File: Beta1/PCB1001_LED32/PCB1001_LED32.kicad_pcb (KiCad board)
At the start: 2 copper layers, 188.9 x 15.5 mm, 164 parts, among them U0 APA102C, U1 APA102C, U10 APA102C, U11 APA102C, U12 APA102C, U13 APA102C, U14 APA102C, U15 APA102C, U16 APA102C, U17 APA102C, U18 APA102C, U19 APA102C, U2 APA102C, U20 APA102C, U21 APA102C, U22 APA102C, U23 APA102C, U24 APA102C, U25 APA102C, U26 APA102C, U27 APA102C, U28 APA102C, U29 APA102C, U3 APA102C, U30 APA102C, U31 APA102C, U4 APA102C, U5 APA102C, U6 APA102C, U7 APA102C, U8 APA102C, U9 APA102C

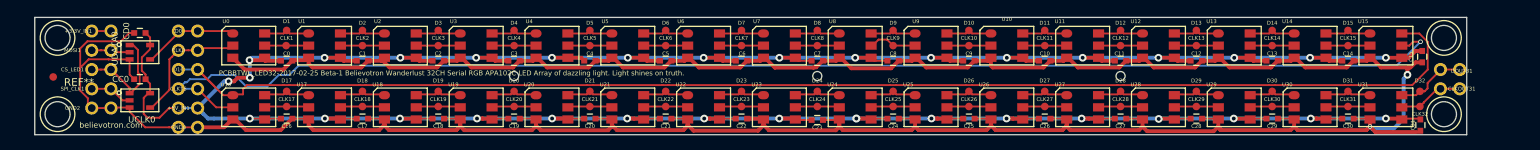
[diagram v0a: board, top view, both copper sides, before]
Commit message: Mid reroute. Move interference. Clean silk.
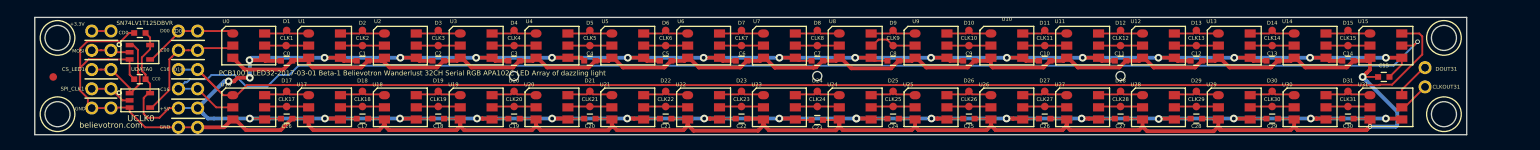
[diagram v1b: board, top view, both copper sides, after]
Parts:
- removed C31: 0.1u, Capacitors_SMD:C_0603
- removed CLK32, D32: CONN_01X01, Liberry:TESTPAD
- removed CLKOUTB31, DOUTB31: CONN_01X01, Liberry:single_0.1
- moved C15 5.73 mm to (180.5, -7.62), turned to 180 degrees
- moved CLKOUT31 2.05 mm to (185.8, -6.31)
- moved DOUT31 2.05 mm to (185.8, -8.67)
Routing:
- net GND: track 453.0 -> 443.0 mm
- net /D32: track 9.69 -> 5.15 mm
- net /CLK32: track 8.56 -> 4.39 mm
- net /D16: track 179.1 -> 176.6 mm
- net +5V: track 478.8 -> 476.8 mm
- net /CLK16: track 178.5 -> 177.7 mm
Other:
- board text added: "+3.3V"
- board text added: "+5V"
- board text added: "C00"
- board text added: "C16"
- board text added: "D00"
- board text added: "GND"
- board text added: "MOSI"
- board text added: "PCB1001_LED32-2017-03-01 Beta-1 Believotron Wanderlust 32CH Serial RGB APA102C LED Array of dazzling light"
- board text added: "Primary CS (Chip Select) wired to Micro To add downstream daisy chain PCBs Tie CS to GND Skip Buffers if using 5V logic"
- board text added: "SN74LV1T125DBVR"
- board text removed: "PCBBTWL_LED32-2017-02-25 Beta-1 Believotron Wanderlust 32CH Serial RGB APA102C LED Array of dazzling light. Light shines on truth."

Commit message: Added labels on bottom. Added CS short to GND.
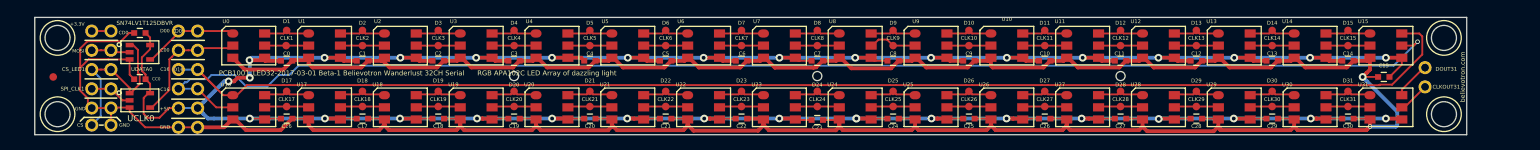
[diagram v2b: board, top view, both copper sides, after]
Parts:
- added CS_LED1: CONN_01X01, Liberry:single_0.1, F.Cu at (10.1, -1.27)
- added GNDB2: CONN_01X01, Liberry:single_0.1, F.Cu at (12.6, -1.27)
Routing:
- net Net-(CS_LED1-Pad1): track 14.5 -> 22.8 mm
- net GND: track 443.0 -> 445.3 mm
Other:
- board text added: "CS"
- board text added: "CS_LED1"
- board text added: "D16"
- board text added: "SPI_CLK_1"
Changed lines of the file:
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@@
 (kicad_pcb (version 4) (host pcbnew 4.0.4-stable)
   (general
-    (links 286)
-    (no_connects 0)
+    (links 282)
+    (no_connects 2)
     (area 2.489999 -15.524901 191.470001 0.050001)
     (thickness 1.6)
-    (drawings 35)
-    (tracks 771)
+    (drawings 52)
+    (tracks 776)
     (zones 0)
-    (modules 159)
+    (modules 161)
     (nets 73)
   )
@@
     (add_net "Net-(SPI_CLK1-Pad1)")
   )
+  (module Liberry:single_0.1 (layer F.Cu)
+    (at 12.59 -1.27)
+    (descr "10 pins through hole IDC header")
+    (tags "IDC header socket VASCH")
+    (fp_text reference GNDB2 (at -2.54 0) (layer F.SilkS) hide
+      (effects (font (size 0.5 0.5) (thickness 0.125)))
+    )
+    (fp_text value CONN_01X01 (at 0 2.54) (layer F.Fab)
+      (effects (font (size 1 1) (thickness 0.15)))
+    )
+    (pad 1 thru_hole circle (at 0 0) (size 1.7272 1.7272) (drill 1.016) (layers *.Cu *.Mask)
+      (net 2 GND))
+  )
+  (module Liberry:single_0.1 (layer F.Cu)
+    (at 10.05 -1.27)
+    (descr "10 pins through hole IDC header")
+    (tags "IDC header socket VASCH")
+    (fp_text reference CS_LED1 (at -1.016 0) (layer F.SilkS) hide
+      (effects (font (size 0.5 0.5) (thickness 0.125)))
+    )
+    (fp_text value CONN_01X01 (at 0 2.54) (layer F.Fab)
+      (effects (font (size 0.5 0.5) (thickness 0.125)))
+    )
+    (pad 1 thru_hole circle (at 0 0) (size 1.7272 1.7272) (drill 1.016) (layers *.Cu *.Mask)
+      (net 68 "Net-(CS_LED1-Pad1)"))
+  )
   (module Liberry:PLCC6-1.6x4.2_LED (layer F.Cu)
     (at 160.76 -3.6124)
@@
   (module Liberry:TESTPAD (layer F.Cu)
     (at 65.76 -5.7218)
-    (fp_text reference D20 (at 0 -1.4125) (layer F.SilkS)
+    (fp_text reference D20 (at 0 -0.8822) (layer F.SilkS)
       (effects (font (size 0.5 0.5) (thickness 0.125)))
     )
@@
   (module Liberry:TESTPAD (layer F.Cu)
     (at 105.76 -5.7218)
-    (fp_text reference D24 (at 0 -1.4125) (layer F.SilkS)
+    (fp_text reference D24 (at 0 -0.8822) (layer F.SilkS)
       (effects (font (size 0.5 0.5) (thickness 0.125)))
     )
@@
   (module Liberry:TESTPAD (layer F.Cu)
     (at 145.76 -5.7218)
-    (fp_text reference D28 (at 0 -1.4125) (layer F.SilkS)
+    (fp_text reference D28 (at 0 -0.8822) (layer F.SilkS)
       (effects (font (size 0.5 0.5) (thickness 0.125)))
     )
@@
       (solder_mask_margin 0.77) (clearance 0.77))
   )
+  (gr_line (start 11.066 -1.27) (end 11.574 -1.27) (layer F.SilkS) (width 0.2))
+  (gr_line (start 9.034 -2.286) (end 8.526 -1.778) (layer F.SilkS) (width 0.2))
+  (gr_line (start 13.352 -2.286) (end 13.86 -1.778) (layer F.SilkS) (width 0.2))
+  (gr_line (start 9.034 -2.286) (end 13.352 -2.286) (layer F.SilkS) (width 0.2))
+  (gr_text GND (at 14.368 -1.27) (layer F.SilkS)
+    (effects (font (size 0.45 0.45) (thickness 0.1)))
+  )
+  (gr_text CS (at 8.526 -1.27) (layer F.SilkS)
+    (effects (font (size 0.45 0.45) (thickness 0.1)))
+  )
+  (gr_text GND (at 8.526 -3.556) (layer B.SilkS)
+    (effects (font (size 0.45 0.45) (thickness 0.1)) (justify mirror))
+  )
+  (gr_text SPI_CLK_1 (at 7.256 -6.096) (layer B.SilkS)
+    (effects (font (size 0.45 0.45) (thickness 0.1)) (justify mirror))
+  )
+  (gr_text CS_LED1 (at 7.51 -8.636) (layer B.SilkS)
+    (effects (font (size 0.45 0.45) (thickness 0.1)) (justify mirror))
+  )
+  (gr_text MOSI (at 8.272 -10.922) (layer B.SilkS)
+    (effects (font (size 0.45 0.45) (thickness 0.1)) (justify mirror))
+  )
+  (gr_text +3.3V (at 8.272 -14.732) (layer B.SilkS)
+    (effects (font (size 0.45 0.45) (thickness 0.1)) (justify mirror))
+  )
+  (gr_text GND (at 25.798 -1.016) (layer B.SilkS)
+    (effects (font (size 0.45 0.45) (thickness 0.1)) (justify mirror))
+  )
+  (gr_text +5V (at 25.798 -3.556) (layer B.SilkS)
+    (effects (font (size 0.45 0.45) (thickness 0.1)) (justify mirror))
+  )
+  (gr_text C16 (at 25.798 -6.096) (layer B.SilkS)
+    (effects (font (size 0.45 0.45) (thickness 0.1)) (justify mirror))
+  )
+  (gr_text D16 (at 25.798 -8.636) (layer B.SilkS)
+    (effects (font (size 0.45 0.45) (thickness 0.1)) (justify mirror))
+  )
+  (gr_text C00 (at 26.052 -11.176) (layer B.SilkS)
+    (effects (font (size 0.45 0.45) (thickness 0.1)) (justify mirror))
+  )
+  (gr_text D00 (at 26.052 -13.716) (layer B.SilkS)
+    (effects (font (size 0.45 0.45) (thickness 0.1)) (justify mirror))
+  )
   (gr_text D00 (at 19.702 -13.716) (layer F.SilkS)
     (effects (font (size 0.45 0.45) (thickness 0.1)))
@@
     (effects (font (size 0.45 0.45) (thickness 0.1)))
   )
-  (gr_text +3.3V (at 8.145 -14.605 360) (layer F.SilkS)
+  (gr_text +3.3V (at 8.145 -14.605) (layer F.SilkS)
     (effects (font (size 0.45 0.45) (thickness 0.1)))
   )
-  (gr_text believotron.com (at 12.59 -1.27) (layer F.SilkS)
-    (effects (font (size 0.75 0.75) (thickness 0.1875)))
+  (gr_text believotron.com (at 190.898 -7.62 90) (layer F.SilkS)
+    (effects (font (size 0.6 0.6) (thickness 0.15)))
   )
-  (gr_text "PCB1001_LED32-2017-03-01 Beta-1 Believotron Wanderlust 32CH Serial RGB APA102C LED Array of dazzling light\n" (at 26.814 -8.128) (layer F.SilkS)
+  (gr_text "PCB1001_LED32-2017-03-01 Beta-1 Believotron Wanderlust 32CH Serial      RGB APA102C LED Array of dazzling light\n" (at 26.814 -8.128) (layer F.SilkS)
     (effects (font (size 0.65 0.65) (thickness 0.125)) (justify left))
   )
@@
   (segment (start 182.86 -10.1531) (end 180.76 -10.1531) (width 0.508) (layer F.Cu) (net 1) (status 10))
   (via (at 180.76 -10.1531) (size 1.016) (drill 0.508) (layers F.Cu B.Cu) (net 1))
+  (segment (start 12.59 -3.5162) (end 12.59 -1.27) (width 0.25) (layer F.Cu) (net 2))
   (segment (start 179.722 -7.62) (end 177.690006 -7.62) (width 0.25) (layer F.Cu) (net 2))
   (segment (start 182.261999 -1.269999) (end 182.261999 -3.048007) (width 0.508) (layer B.Cu) (net 2))
@@
   (segment (start 182.7506 -5.3218) (end 182.86 -5.2124) (width 0.25) (layer F.Cu) (net 66))
   (segment (start 12.59 -13.6762) (end 10.05 -13.6762) (width 0.25) (layer F.Cu) (net 67))
+  (segment (start 10.05 -1.27) (end 11.238601 -2.458601) (width 0.25) (layer B.Cu) (net 68))
+  (segment (start 11.238601 -2.458601) (end 11.238601 -7.407599) (width 0.25) (layer B.Cu) (net 68))
+  (segment (start 11.238601 -7.407599) (end 10.913599 -7.732601) (width 0.25) (layer B.Cu) (net 68))
+  (segment (start 10.913599 -7.732601) (end 10.05 -8.5962) (width 0.25) (layer B.Cu) (net 68))
   (segment (start 10.05 -8.5962) (end 11.271314 -8.5962) (width 0.25) (layer F.Cu) (net 68))
   (segment (start 11.271314 -8.5962) (end 12.59 -8.5962) (width 0.25) (layer F.Cu) (net 68))

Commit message: Changed from 36U to 38U. Ready for Fab.
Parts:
- added REF**: Fiducial_1mm_Dia_2.54mm_Outer_CopperTop, Fiducials:Fiducial_1mm_Dia_2.54mm_Outer_CopperTop, F.Cu at (196.0, -7.74)
- moved REF** 7.62 mm to (196.0, -12.8)
- moved REF** 7.62 mm to (196.0, -2.71)
- moved CS_LED1 7.13 mm to (13.2, -7.69)
- moved +5V_IN1 3.13 mm to (27.1, -3.88)
- moved +5V_INB1 3.13 mm to (24.6, -3.88)
- moved CLK16 3.13 mm to (27.1, -6.42)
- moved CLKB16 3.13 mm to (24.6, -6.42)
- moved D0 3.13 mm to (27.1, -14.0)
- moved D16 3.13 mm to (27.1, -8.96)
- moved DB0 3.13 mm to (24.6, -14.0)
- moved DB16 3.13 mm to (24.6, -8.96)
- moved GND0 3.13 mm to (27.1, -1.34)
- moved GNDB0 3.13 mm to (24.6, -1.34)
- moved CLK0 3.13 mm to (27.1, -11.5)
- moved CLKB0 3.13 mm to (24.6, -11.5)
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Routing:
- net GND: track 445.3 -> 459.1 mm
- net Net-(MOSI1-Pad1): track 5.11 -> 9.95 mm
- net Net-(SPI_CLK1-Pad1): track 5.63 -> 9.77 mm
- net Net-(CS_LED1-Pad1): track 22.8 -> 18.8 mm
- net /CLK16: track 177.7 -> 174.2 mm
- net /D16: track 176.6 -> 173.6 mm
- net /CLK: track 16.7 -> 17.4 mm
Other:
- board size 188.9 x 15.5 mm -> 199 x 15.5 mm
- board text added: "CLKOUT31"
- board text added: "DOUT31"
- board text added: "Open source MIT license files at: github.com/Believotron/BelievotronWanderlustHardware Replacement parts, upgrades, updates, new gear, and marketing pap: Believotron.com For help, bug reporting, dev-blogs, or joy at your bonkers-cool creation, the good stuff is here: community.believotron.com"
- board text added: "PCB1001_LED32-2017-03-31 Beta-1 Believotron Wanderlust 32CH Serial RGB APA102C LED Array of dazzling light"
- board text added: "Test procedure: Test R between +3.3V, +5V; Test R between +3.3V, GND; Test R between +5V, GND; For each LED { Test R between each CLK[i], D[i]; Test R between each CLK[i], GND; Test R between each CLK[i], +5V; } Debug: Use logic analyzer on buffers. (USE CORRECT VOLTAGE LEVEL)"
- board text added: "The most definitive information on the APA102C is from your supplier, but this guy seems to have more: https://cpldcpu.com/2014/08/27/apa102/"
- board text removed: "CS"
- board text removed: "PCB1001_LED32-2017-03-01 Beta-1 Believotron Wanderlust 32CH Serial RGB APA102C LED Array of dazzling light"
